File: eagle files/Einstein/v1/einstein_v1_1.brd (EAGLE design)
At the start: 160 x 100 mm, 11 parts, among them U2 ADXL345PATRICK

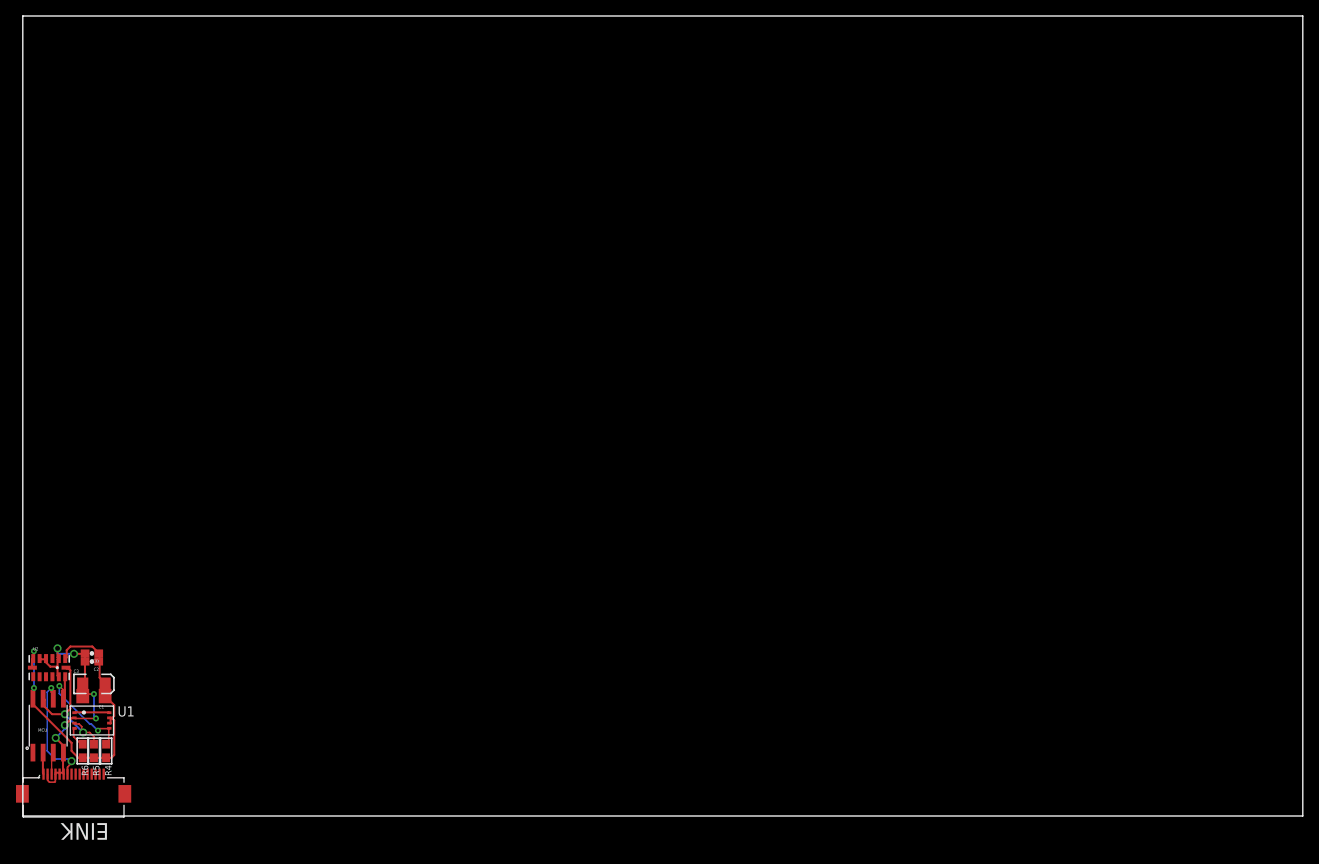
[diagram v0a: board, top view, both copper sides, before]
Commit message: Added  coil for NFC power transfer
Added  coil for NFC power transfer
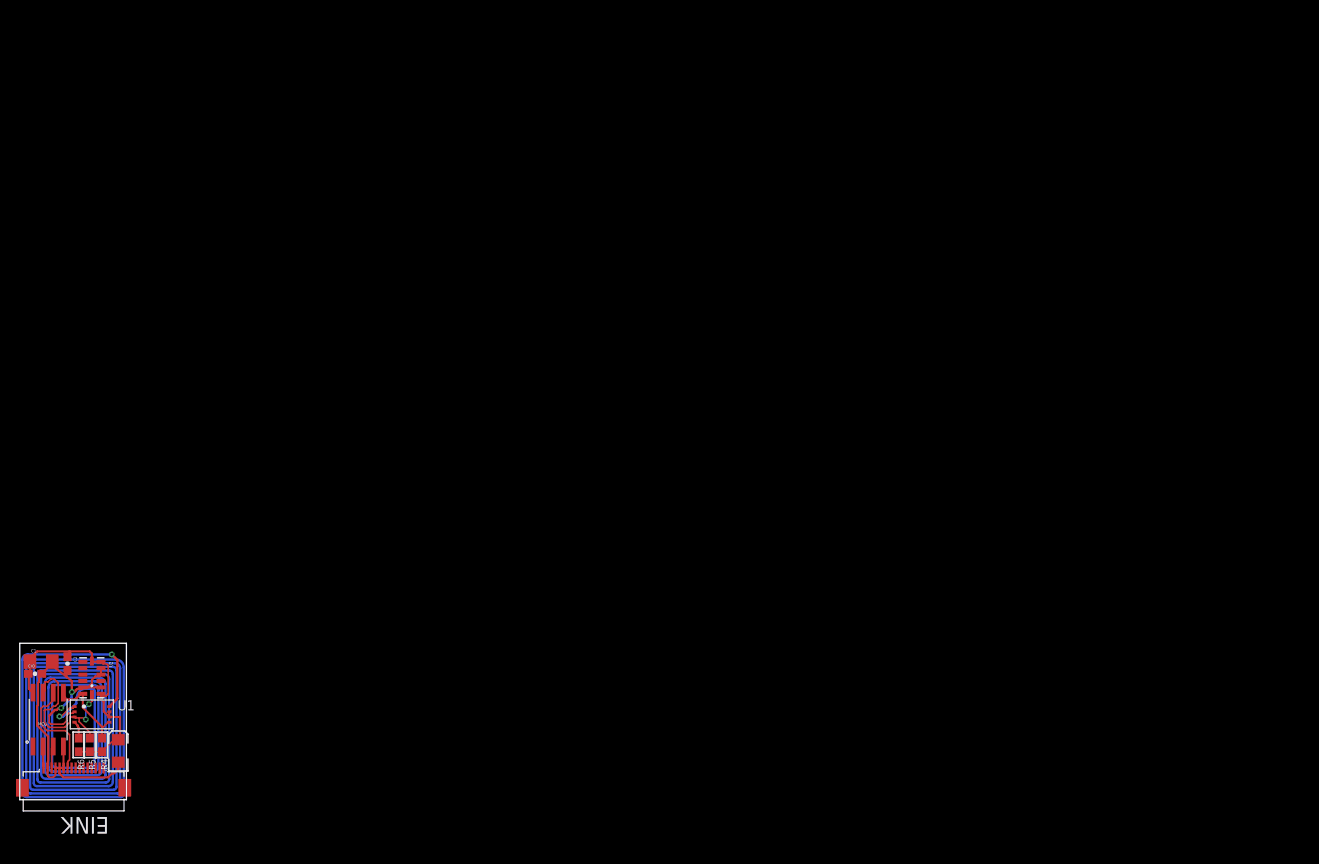
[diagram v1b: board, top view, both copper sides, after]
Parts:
- moved C3 8.92 mm to (11.9, 8.13), turned to 90 degrees
- moved C1 7.89 mm to (2.29, 19.3), turned to 0 degrees
- moved CIO 7.55 mm to (1.52, 17.8), turned to 0 degrees
- moved U2 5.48 mm to (8.64, 17.3), turned to 270 degrees
- moved C2 3.06 mm to (5.59, 19.1), turned to 270 degrees
- moved R5 0.92 mm to (8.38, 8.89)
- moved R6 0.92 mm to (6.99, 8.89)
- moved R4 0.92 mm to (9.91, 8.89)
- moved EINK 0.76 mm to (6.35, 8.89)
- moved MCU 0.76 mm to (3.17, 12.1)
- moved U1 0.76 mm to (8.64, 12.7)
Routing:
- net COIL: track 4.37 -> 416.4 mm, vias 0 -> 2
- net GND: track 36.3 -> 55.7 mm, vias 6 -> 2
- net VCC: track 45.2 -> 39.7 mm, vias 2 -> 0
- net CLOCK: track 18.1 -> 23.2 mm
- net DATA: track 15.5 -> 13.2 mm, vias 2 -> 0
- net DOT5: track 14.9 -> 13.3 mm, vias 2 -> 0
- net FD: track 2.81 -> 2.20 mm
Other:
- board size 160 x 100 mm -> 13.3 x 19.6 mm
